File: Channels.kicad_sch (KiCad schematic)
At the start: 24 parts, among them J1 Pullup_Sel, J3 Wiegand, Q1 2N7002, Q2 2N7002

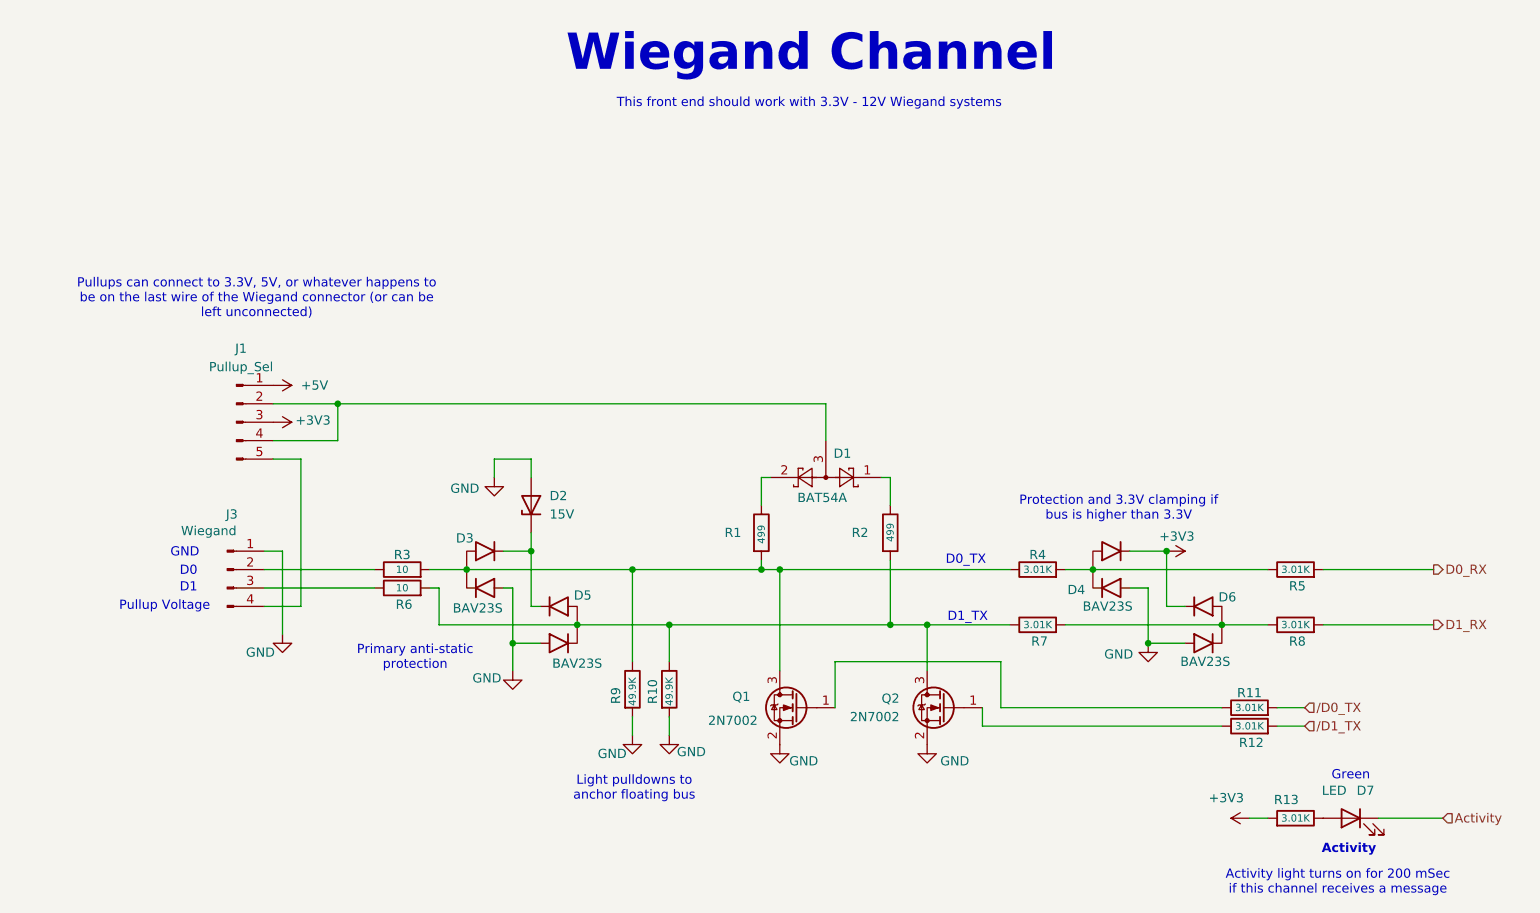
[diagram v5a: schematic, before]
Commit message: BOM now has added JLCPCB data; gerbers and drill info created for JLC. This rev was ordered from JLCPCB on this day.
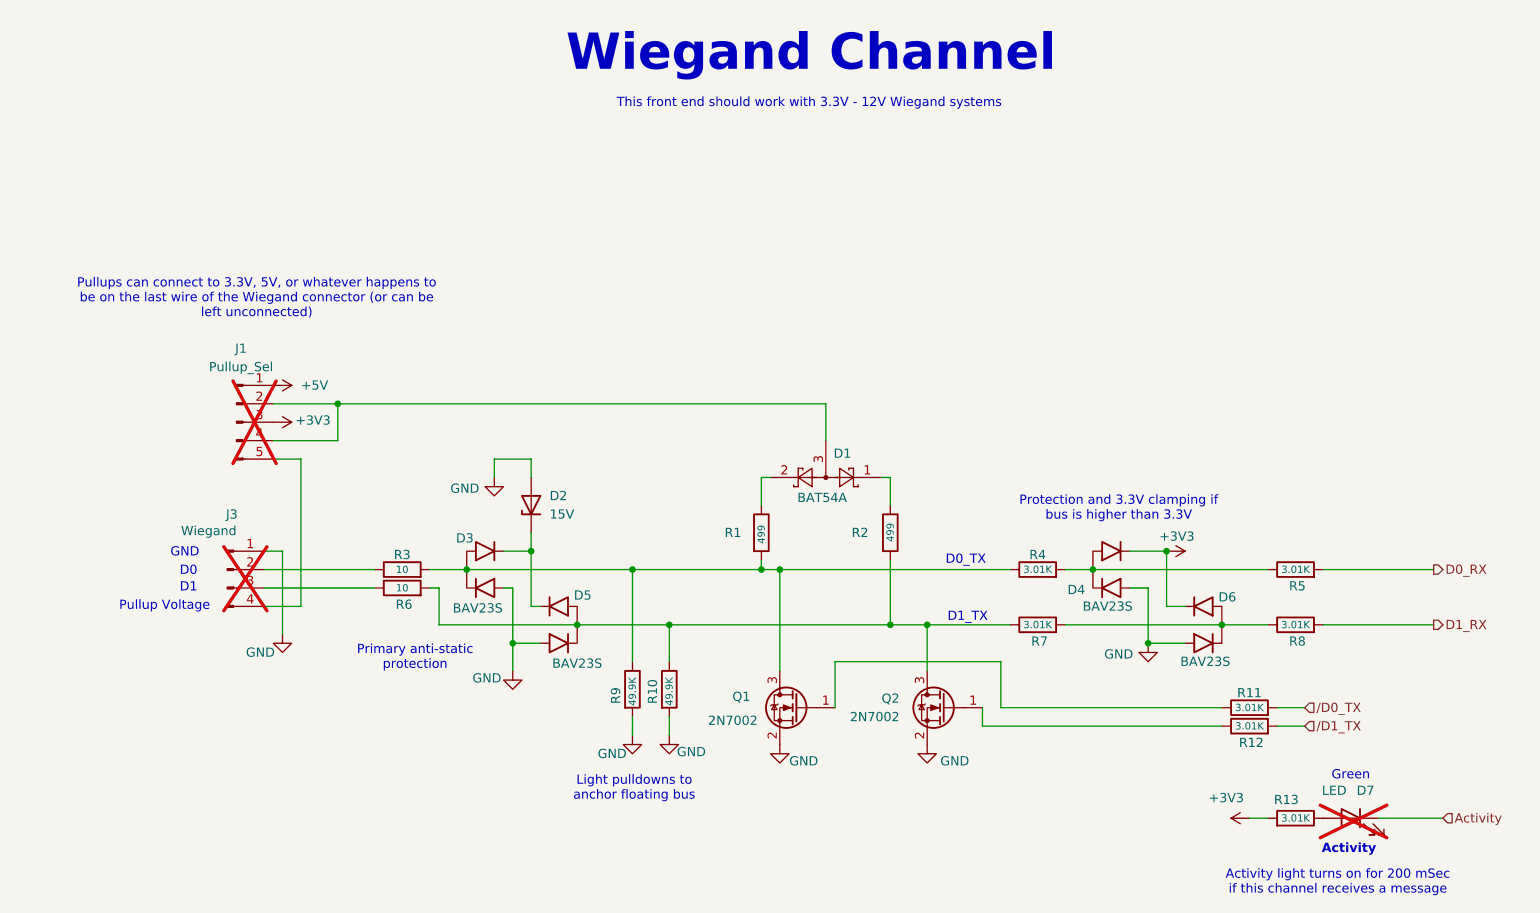
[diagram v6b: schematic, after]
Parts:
- D1: JLCPCB Part Number (none) -> C8591
- D2: JLCPCB Part Number (none) -> C460772
- D3, D4, D5, D6: JLCPCB Part Number (none) -> C44345
- D7, J1, J3: JLCPCB Part Number (none) -> N/A; now not fitted
- Q1, Q2: JLCPCB Part Number (none) -> C16338
- R1, R2: JLCPCB Part Number (none) -> C23065
- R10, R9: JLCPCB Part Number (none) -> C22356488
- R11, R12, R13, R4, R5, R7, R8: JLCPCB Part Number (none) -> C22356559
- R3, R6: JLCPCB Part Number (none) -> C177346
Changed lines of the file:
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@@
 		(in_bom yes)
 		(on_board yes)
-		(dnp no)
+		(dnp yes)
 		(fields_autoplaced yes)
 		(property "Reference" "J1"
@@
 			)
 		)
+		(property "JLCPCB Part Number" "N/A"
+			(at 59.69 78.74 0)
+			(effects
+				(font
+					(size 1.27 1.27)
+				)
+				(hide yes)
+			)
+		)
 		(pin "4"
 		)
@@
 			)
 		)
+		(property "JLCPCB Part Number" "C22356559"
+			(at 170.18 99.06 0)
+			(effects
+				(font
+					(size 1.27 1.27)
+				)
+				(hide yes)
+			)
+		)
 		(pin "2"
 		)
@@
 			)
 		)
+		(property "JLCPCB Part Number" "C44345"
+			(at 107.95 106.68 0)
+			(effects
+				(font
+					(size 1.27 1.27)
+				)
+				(hide yes)
+			)
+		)
 		(pin "2"
 		)
@@
 			)
 		)
+		(property "JLCPCB Part Number" "C44345"
+			(at 90.17 99.06 0)
+			(effects
+				(font
+					(size 1.27 1.27)
+				)
+				(hide yes)
+			)
+		)
 		(pin "2"
 		)
@@
 			)
 		)
+		(property "JLCPCB Part Number" "C44345"
+			(at 196.85 106.68 0)
+			(effects
+				(font
+					(size 1.27 1.27)
+				)
+				(hide yes)
+			)
+		)
 		(pin "2"
 		)
@@
 			)
 		)
+		(property "JLCPCB Part Number" "C177346"
+			(at 82.55 101.6 0)
+			(effects
+				(font
+					(size 1.27 1.27)
+				)
+				(hide yes)
+			)
+		)
 		(pin "2"
 		)
@@
 			)
 		)
+		(property "JLCPCB Part Number" "C22356488"
+			(at 114.3 115.57 0)
+			(effects
+				(font
+					(size 1.27 1.27)
+				)
+				(hide yes)
+			)
+		)
 		(pin "2"
 		)
@@
 			)
 		)
+		(property "JLCPCB Part Number" "C8591"
+			(at 140.97 86.36 0)
+			(effects
+				(font
+					(size 1.27 1.27)
+				)
+				(hide yes)
+			)
+		)
 		(pin "3"
 		)
@@
 			)
 		)
+		(property "JLCPCB Part Number" "C22356559"
+			(at 199.39 118.11 0)
+			(effects
+				(font
+					(size 1.27 1.27)
+				)
+				(hide yes)
+			)
+		)
 		(pin "2"
 		)
@@
 			)
 		)
+		(property "JLCPCB Part Number" "C22356488"
+			(at 119.38 115.57 0)
+			(effects
+				(font
+					(size 1.27 1.27)
+				)
+				(hide yes)
+			)
+		)
 		(pin "2"
 		)
@@
 			)
 		)
+		(property "JLCPCB Part Number" "C22356559"
+			(at 205.74 106.68 0)
+			(effects
+				(font
+					(size 1.27 1.27)
+				)
+				(hide yes)
+			)
+		)
 		(pin "2"
 		)
@@
 		(in_bom yes)
 		(on_board yes)
-		(dnp no)
+		(dnp yes)
 		(property "Reference" "D7"
 			(at 215.392 129.54 0)
@@
 			)
 		)
+		(property "JLCPCB Part Number" "N/A"
+			(at 213.36 133.35 0)
+			(effects
+				(font
+					(size 1.27 1.27)
+				)
+				(hide yes)
+			)
+		)
 		(pin "2"
 		)
@@
 			)
 		)
+		(property "JLCPCB Part Number" "C22356559"
+			(at 205.74 133.35 0)
+			(effects
+				(font
+					(size 1.27 1.27)
+				)
+				(hide yes)
+			)
+		)
 		(pin "2"
 		)
@@
 			)
 		)
+		(property "JLCPCB Part Number" "C16338"
+			(at 137.16 118.11 0)
+			(effects
+				(font
+					(size 1.27 1.27)
+				)
+				(hide yes)
+			)
+		)
 		(pin "2"
 		)
@@
 			)
 		)
+		(property "JLCPCB Part Number" "C460772"
+			(at 100.33 90.17 0)
+			(effects
+				(font
+					(size 1.27 1.27)
+				)
+				(hide yes)
+			)
+		)
 		(pin "1"
 		)
@@
 			)
 		)
+		(property "JLCPCB Part Number" "C23065"
+			(at 149.86 93.98 0)
+			(effects
+				(font
+					(size 1.27 1.27)
+				)
+				(hide yes)
+			)
+		)
 		(pin "2"
 		)
@@
 			)
 		)
+		(property "JLCPCB Part Number" "C16338"
+			(at 157.48 118.11 0)
+			(effects
+				(font
+					(size 1.27 1.27)
+				)
+				(hide yes)
+			)
+		)
 		(pin "2"
 		)
@@
 			)
 		)
+		(property "JLCPCB Part Number" "C44345"
+			(at 176.53 99.06 0)
+			(effects
+				(font
+					(size 1.27 1.27)
+				)
+				(hide yes)
+			)
+		)
 		(pin "2"
 		)
@@
 		(in_bom yes)
 		(on_board yes)
-		(dnp no)
+		(dnp yes)
 		(property "Reference" "J3"
 			(at 59.055 91.44 0)
@@
 			)
 		)
+		(property "JLCPCB Part Number" "N/A"
+			(at 58.42 99.06 0)
+			(effects
+				(font
+					(size 1.27 1.27)
+				)
+				(hide yes)
+			)
+		)
 		(pin "1"
 		)
@@
 			)
 		)
+		(property "JLCPCB Part Number" "C22356559"
+			(at 199.39 120.65 0)
+			(effects
+				(font
+					(size 1.27 1.27)
+				)
+				(hide yes)
+			)
+		)
 		(pin "2"
 		)
@@
 			)
 		)
+		(property "JLCPCB Part Number" "C177346"
+			(at 82.55 99.06 0)
+			(effects
+				(font
+					(size 1.27 1.27)
+				)
+				(hide yes)
+			)
+		)
 		(pin "2"
 		)
@@
 			)
 		)
+		(property "JLCPCB Part Number" "C22356559"
+			(at 170.18 106.68 0)
+			(effects
+				(font
+					(size 1.27 1.27)
+				)
+				(hide yes)
+			)
+		)
 		(pin "2"
 		)
@@
 			)
 		)
+		(property "JLCPCB Part Number" "C23065"
+			(at 132.08 93.98 0)
+			(effects
+				(font
+					(size 1.27 1.27)
+				)
+				(hide yes)
+			)
+		)
 		(pin "2"
 		)
@@
 			(at 205.74 99.06 0)
 			(effects
+				(font
+					(size 1.27 1.27)
+				)
+				(hide yes)
+			)
+		)
+		(property "JLCPCB Part Number" "C22356559"
+			(at 205.74 99.06 0)
+			(effects
